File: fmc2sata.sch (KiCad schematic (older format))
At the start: 31 parts, among them J1 ASP-134488-01, J2 1-2199230-6, U1 TPS565208, U2 TPS565208

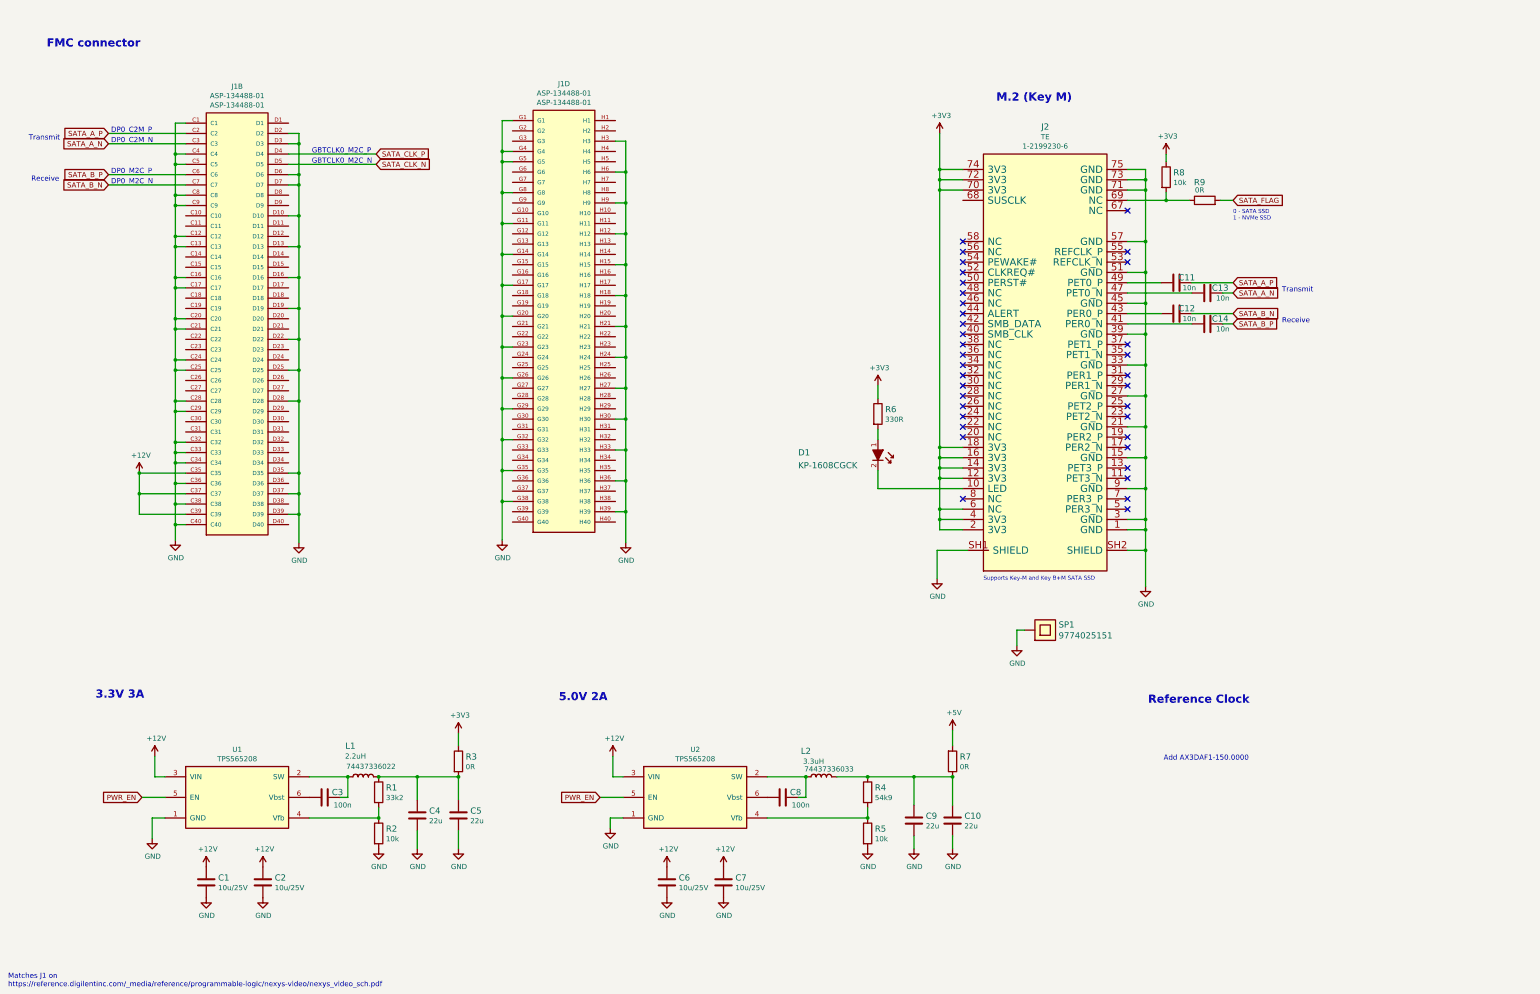
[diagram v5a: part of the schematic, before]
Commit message: Add 2.5" SATA connector and 150MHz LVDS REF CLK generator
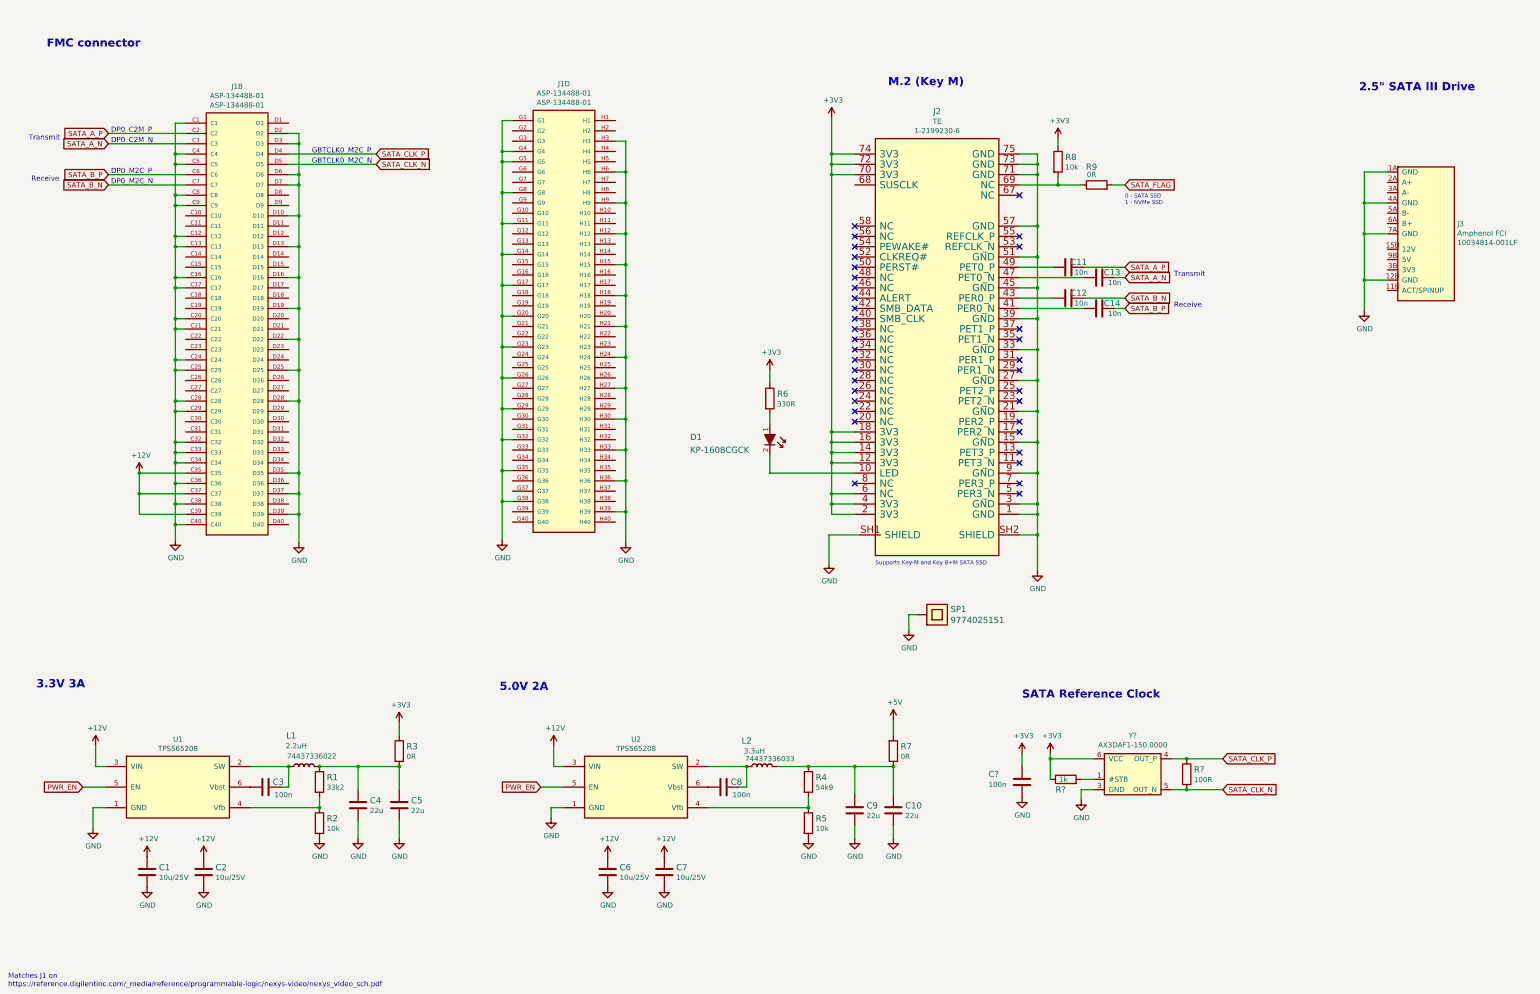
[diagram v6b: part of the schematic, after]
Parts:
- added C?: C_100n_0402, antmicro-footprints:0402-cap, symbol antmicroCapacitors0402:C_100n_0402
- added J3: 10034814-001LF, antmicro-footprints:10034814-001LF, symbol antmicroSATAConnectors:10034814-001LF
- added R?: R_1k_0402, antmicro-footprints:0402-res, symbol antmicroResistors0402:R_1k_0402
- added R?: R_100R_0402, antmicro-footprints:0402-res, symbol antmicroResistors0402:R_100R_0402
- added Y?: AX3DAF1-150.0000, antmicro-footprints:AX3DAF1, symbol antmicroOscillators:AX3DAF1-150.0000
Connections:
- net +3V3: now also C?.1, R?.1, Y?.6 (VCC)
- net GND: now also C?.2, J3.10B (GND), J3.12B (GND), J3.1A (GND), J3.4A (GND), J3.4B (GND), J3.5B (GND), J3.6B (GND), J3.7A (GND), Y?.3 (GND)
- net SATA_CLK_N: now also R?.2, Y?.5 (OUT_N)
- net SATA_CLK_P: now also R?.1, Y?.4 (OUT_P)
- new net: J3.13B (12V), J3.14B (12V), J3.15B (12V)
- new net: J3.1B (3V3), J3.2B (3V3), J3.3B (3V3)
- new net: J3.7B (5V), J3.8B (5V), J3.9B (5V)
- new net: R?.2, Y?.1 (#STB)
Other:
- note added: "2.5" SATA III Drive"
- note added: "SATA Reference Clock"
- note removed: "Add AX3DAF1-150.0000"
- note removed: "Reference Clock"
- moved on the sheet: C1, C10, C11, C12, C13, C14, C2, C3, C4, C5, C6, C7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

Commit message: Cleanup
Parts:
- removed C11: C_10n_0402, antmicro-footprints:0402-cap, symbol antmicroCapacitors0402:C_10n_0402
- added C15, C16, C17, C18, C19: C_10n_0402, antmicro-footprints:0402-cap, symbol antmicroCapacitors0402:C_10n_0402
- gave numbers to parts that had none: 4
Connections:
- net +12V: now also J3.13B (12V), J3.14B (12V), J3.15B (12V)
- net +3V3: now also J3.1B (3V3), J3.2B (3V3), J3.3B (3V3)
- net +5V: now also J3.7B (5V), J3.8B (5V), J3.9B (5V)
- net SATA_A_N: now also C14.1, C18.1; no longer C13.1
- net SATA_A_P: now also C12.1, C16.1
- net SATA_B_N: now also C13.1, C17.1; no longer C12.1
- net SATA_B_P: now also C15.1, C19.1; no longer C14.1
- net M2_SATA_A_N: now reaches C14.2
- net M2_SATA_A_N: now also J2.47 (PET0_N); no longer J2.41 (PER0_N)
- net M2_SATA_A_P: now reaches C12.2
- net M2_SATA_A_P: now also J2.49 (PET0_P); no longer J2.43 (PER0_P)
- net M2_SATA_B_N: now reaches C13.2
- net M2_SATA_B_N: now also J2.43 (PER0_P); no longer J2.47 (PET0_N)
- net EXT_SATA_A_P: now reaches J3.2A (A+)
- net EXT_SATA_A_P: now also C16.2
- net EXT_SATA_A_N: now reaches J3.3A (A-)
- net EXT_SATA_A_N: now also C18.2
- net EXT_SATA_B_N: now reaches J3.5A (B-)
- net EXT_SATA_B_N: now also C17.2
- net EXT_SATA_B_P: now reaches J3.6A (B+)
- net EXT_SATA_B_P: now also C19.2
- new net M2_SATA_B_P: C15.2, J2.41 (PER0_N)
